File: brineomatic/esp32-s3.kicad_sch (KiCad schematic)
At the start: 37 parts, among them J19 USB_TYPE_C_16PIN, J20 Conn_01x04, U5 ESP32-S3-WROOM-1-N16R8, U6 USBLC6-2SC6, U7 LDL1117S33R, U8 SN74LV1T34DBV

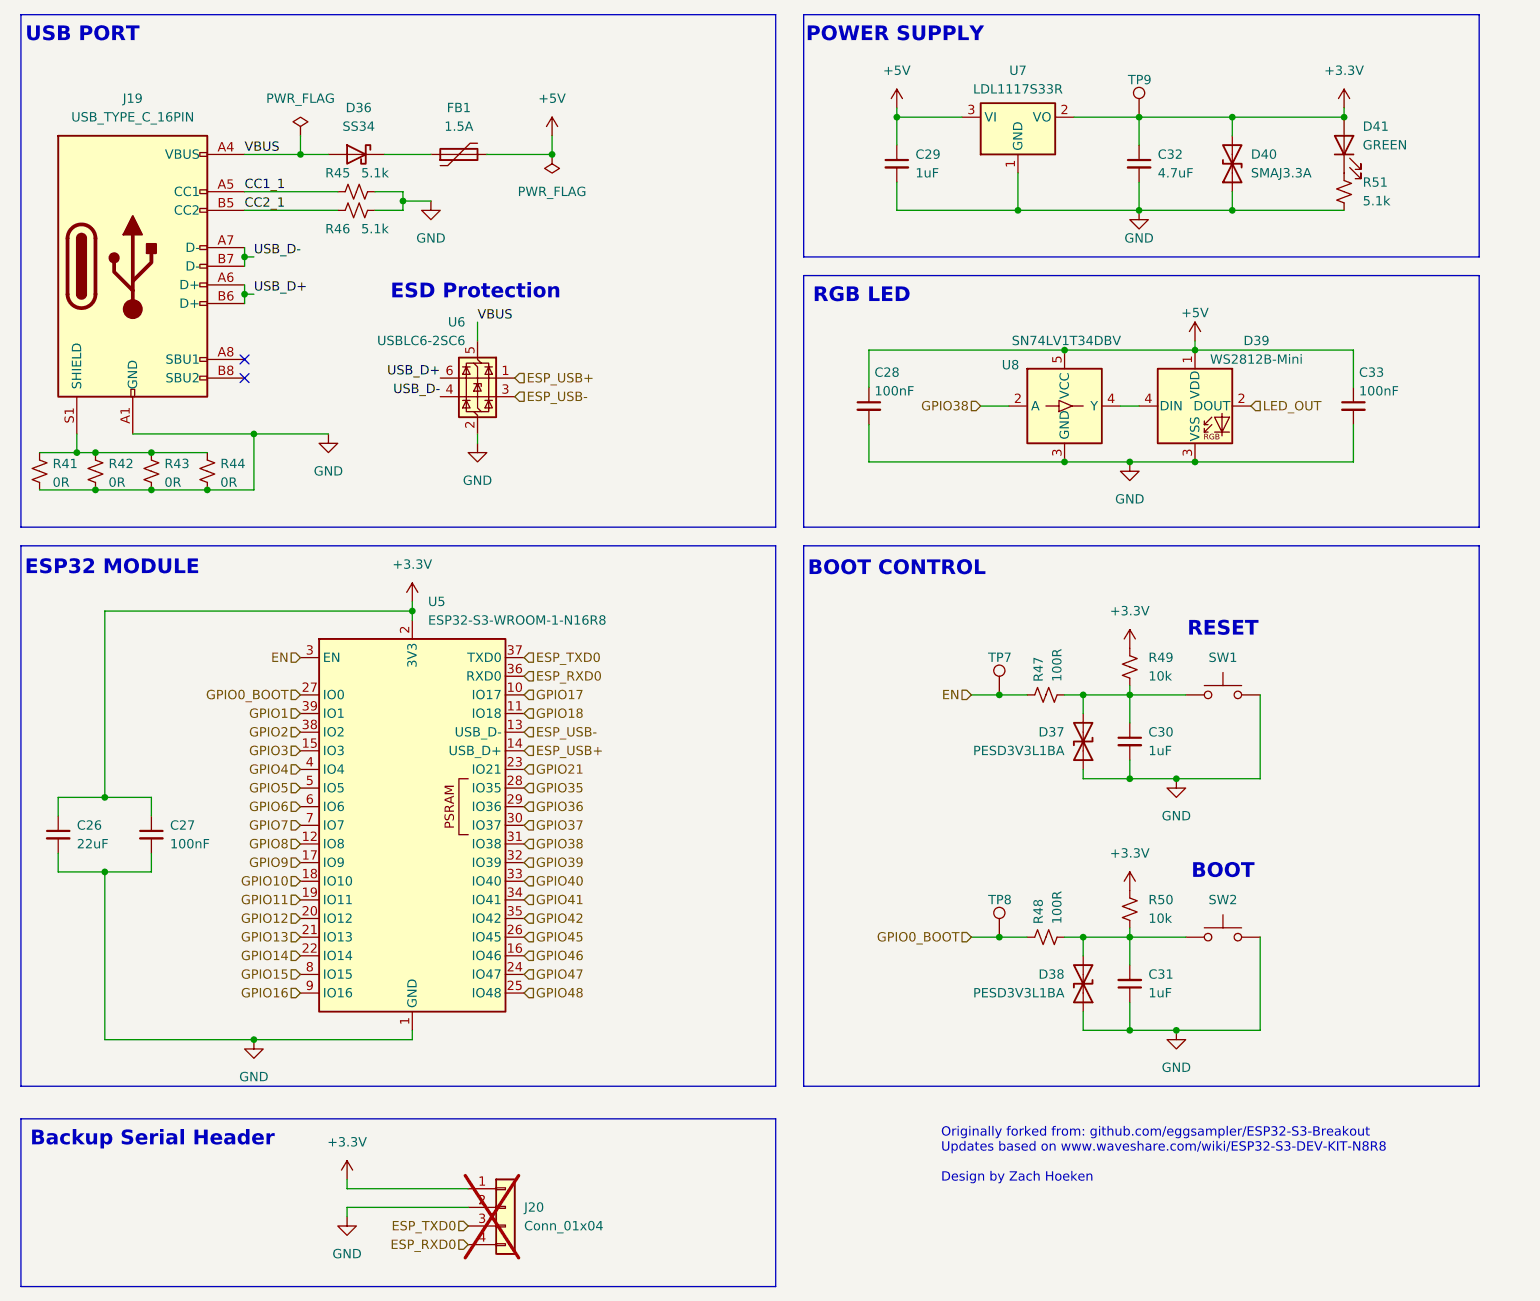
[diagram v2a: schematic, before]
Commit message: updated analog sensor esd schematic
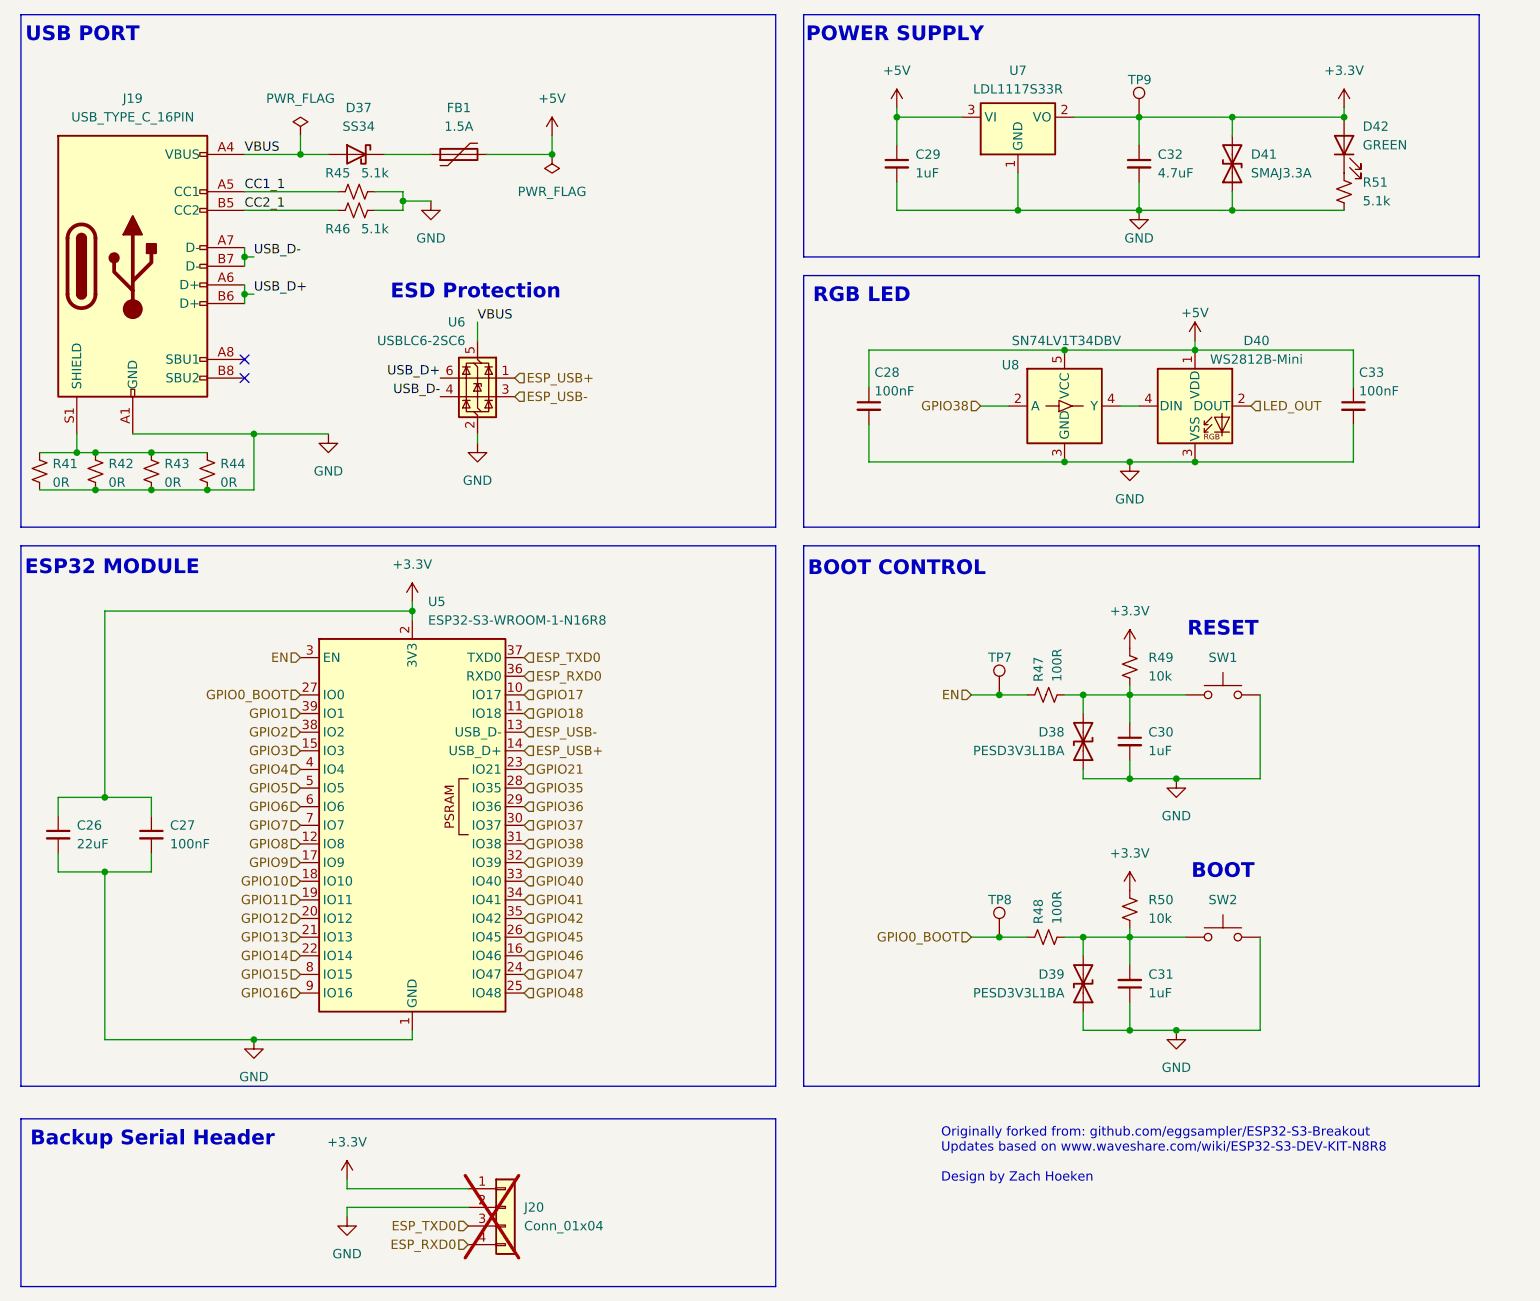
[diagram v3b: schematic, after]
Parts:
- renumbered D36 to D37, D37 to D38, D38 to D39, D39 to D40, D40 to D41, D41 to D42
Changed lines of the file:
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@@
 		(on_board yes)
 		(dnp no)
-		(property "Reference" "#PWR046"
+		(property "Reference" "#PWR047"
 			(at 97.79 179.07 0)
 			(effects
@@
 			(project "brineomatic"
 				(path "/96477ae2-ef08-48f3-8dd4-fe4478541f68/602af921-0504-453c-a784-e82800e98f4c"
-					(reference "#PWR046")
+					(reference "#PWR047")
 					(unit 1)
 				)
@@
 		(on_board yes)
 		(dnp no)
-		(property "Reference" "#PWR054"
+		(property "Reference" "#PWR055"
 			(at 204.47 106.68 0)
 			(effects
@@
 			(project "brineomatic"
 				(path "/96477ae2-ef08-48f3-8dd4-fe4478541f68/602af921-0504-453c-a784-e82800e98f4c"
-					(reference "#PWR054")
+					(reference "#PWR055")
 					(unit 1)
 				)
@@
 		(on_board yes)
 		(dnp no)
-		(property "Reference" "D40"
+		(property "Reference" "D41"
 			(at 220.98 35.56 90)
 			(effects
@@
 			(project "brineomatic"
 				(path "/96477ae2-ef08-48f3-8dd4-fe4478541f68/602af921-0504-453c-a784-e82800e98f4c"
-					(reference "D40")
+					(reference "D41")
 					(unit 1)
 				)
@@
 		(dnp no)
 		(fields_autoplaced yes)
-		(property "Reference" "#PWR050"
+		(property "Reference" "#PWR051"
 			(at 115.57 81.28 0)
 			(effects
@@
 			(project "brineomatic"
 				(path "/96477ae2-ef08-48f3-8dd4-fe4478541f68/602af921-0504-453c-a784-e82800e98f4c"
-					(reference "#PWR050")
+					(reference "#PWR051")
 					(unit 1)
 				)
@@
 		(on_board yes)
 		(dnp no)
-		(property "Reference" "#PWR052"
+		(property "Reference" "#PWR053"
 			(at 172.72 33.02 0)
 			(effects
@@
 			(project "brineomatic"
 				(path "/96477ae2-ef08-48f3-8dd4-fe4478541f68/602af921-0504-453c-a784-e82800e98f4c"
-					(reference "#PWR052")
+					(reference "#PWR053")
 					(unit 1)
 				)
@@
 		(on_board yes)
 		(dnp no)
-		(property "Reference" "#PWR059"
+		(property "Reference" "#PWR060"
 			(at 213.36 64.77 0)
 			(effects
@@
 			(project "brineomatic"
 				(path "/96477ae2-ef08-48f3-8dd4-fe4478541f68/602af921-0504-453c-a784-e82800e98f4c"
-					(reference "#PWR059")
+					(reference "#PWR060")
 					(unit 1)
 				)
@@
 		(on_board yes)
 		(dnp no)
-		(property "Reference" "D38"
+		(property "Reference" "D39"
 			(at 195.58 147.3199 90)
 			(effects
@@
 			(project "brineomatic"
 				(path "/96477ae2-ef08-48f3-8dd4-fe4478541f68/602af921-0504-453c-a784-e82800e98f4c"
-					(reference "D38")
+					(reference "D39")
 					(unit 1)
 				)
@@
 		(on_board yes)
 		(dnp no)
-		(property "Reference" "#PWR055"
+		(property "Reference" "#PWR056"
 			(at 204.47 139.7 0)
 			(effects
@@
 			(project "brineomatic"
 				(path "/96477ae2-ef08-48f3-8dd4-fe4478541f68/602af921-0504-453c-a784-e82800e98f4c"
-					(reference "#PWR055")
+					(reference "#PWR056")
 					(unit 1)
 				)
@@
 		(dnp no)
 		(fields_autoplaced yes)
-		(property "Reference" "#PWR047"
+		(property "Reference" "#PWR048"
 			(at 97.79 186.69 0)
 			(effects
@@
 			(project "brineomatic"
 				(path "/96477ae2-ef08-48f3-8dd4-fe4478541f68/602af921-0504-453c-a784-e82800e98f4c"
-					(reference "#PWR047")
+					(reference "#PWR048")
 					(unit 1)
 				)
@@
 		(dnp no)
 		(fields_autoplaced yes)
-		(property "Reference" "#PWR044"
+		(property "Reference" "#PWR045"
 			(at 85.09 162.56 0)
 			(effects
@@
 			(project "brineomatic"
 				(path "/96477ae2-ef08-48f3-8dd4-fe4478541f68/602af921-0504-453c-a784-e82800e98f4c"
-					(reference "#PWR044")
+					(reference "#PWR045")
 					(unit 1)
 				)
@@
 		(dnp no)
 		(fields_autoplaced yes)
-		(property "Reference" "#PWR053"
+		(property "Reference" "#PWR054"
 			(at 204.47 83.82 0)
 			(effects
@@
 			(project "brineomatic"
 				(path "/96477ae2-ef08-48f3-8dd4-fe4478541f68/602af921-0504-453c-a784-e82800e98f4c"
-					(reference "#PWR053")
+					(reference "#PWR054")
 					(unit 1)
 				)
@@
 		(on_board yes)
 		(dnp no)
-		(property "Reference" "D36"
+		(property "Reference" "D37"
 			(at 99.3775 29.21 0)
 			(effects
@@
 			(project "brineomatic"
 				(path "/96477ae2-ef08-48f3-8dd4-fe4478541f68/602af921-0504-453c-a784-e82800e98f4c"
-					(reference "D36")
+					(reference "D37")
 					(unit 1)
 				)
@@
 		(dnp no)
 		(fields_autoplaced yes)
-		(property "Reference" "#PWR057"
+		(property "Reference" "#PWR058"
 			(at 210.82 127 0)
 			(effects
@@
 			(project "brineomatic"
 				(path "/96477ae2-ef08-48f3-8dd4-fe4478541f68/602af921-0504-453c-a784-e82800e98f4c"
-					(reference "#PWR057")
+					(reference "#PWR058")
 					(unit 1)
 				)
@@
 		(dnp no)
 		(fields_autoplaced yes)
-		(property "Reference" "#PWR058"
+		(property "Reference" "#PWR059"
 			(at 210.82 161.29 0)
 			(effects
@@
 			(project "brineomatic"
 				(path "/96477ae2-ef08-48f3-8dd4-fe4478541f68/602af921-0504-453c-a784-e82800e98f4c"
-					(reference "#PWR058")
+					(reference "#PWR059")
 					(unit 1)
 				)
@@
 		(on_board yes)
 		(dnp no)
-		(property "Reference" "D39"
+		(property "Reference" "D40"
 			(at 221.742 60.96 0)
 			(effects
@@
 			(project "brineomatic"
 				(path "/96477ae2-ef08-48f3-8dd4-fe4478541f68/602af921-0504-453c-a784-e82800e98f4c"
-					(reference "D39")
+					(reference "D40")
 					(unit 1)
 				)
@@
 		(dnp no)
 		(fields_autoplaced yes)
-		(property "Reference" "#PWR049"
+		(property "Reference" "#PWR050"
 			(at 109.22 48.26 0)
 			(effects
@@
 			(project "brineomatic"
 				(path "/96477ae2-ef08-48f3-8dd4-fe4478541f68/602af921-0504-453c-a784-e82800e98f4c"
-					(reference "#PWR049")
+					(reference "#PWR050")
 					(unit 1)
 				)
@@
 		(on_board yes)
 		(dnp no)
-		(property "Reference" "#PWR048"
+		(property "Reference" "#PWR049"
 			(at 106.68 100.33 0)
 			(effects
@@
 			(project "brineomatic"
 				(path "/96477ae2-ef08-48f3-8dd4-fe4478541f68/602af921-0504-453c-a784-e82800e98f4c"
-					(reference "#PWR048")
+					(reference "#PWR049")
 					(unit 1)
 				)
@@
 		(on_board yes)
 		(dnp no)
-		(property "Reference" "#PWR060"
+		(property "Reference" "#PWR061"
 			(at 233.68 33.02 0)
 			(effects
@@
 			(project "brineomatic"
 				(path "/96477ae2-ef08-48f3-8dd4-fe4478541f68/602af921-0504-453c-a784-e82800e98f4c"
-					(reference "#PWR060")
+					(reference "#PWR061")
 					(unit 1)
 				)
@@
 		(on_board yes)
 		(dnp no)
-		(property "Reference" "D41"
+		(property "Reference" "D42"
 			(at 236.22 31.75 90)
 			(effects
@@
 			(project "brineomatic"
 				(path "/96477ae2-ef08-48f3-8dd4-fe4478541f68/602af921-0504-453c-a784-e82800e98f4c"
-					(reference "D41")
+					(reference "D42")
 					(unit 1)
 				)
@@
 		(dnp no)
 		(fields_autoplaced yes)
-		(property "Reference" "#PWR045"
+		(property "Reference" "#PWR046"
 			(at 95.25 80.01 0)
 			(effects
@@
 			(project "brineomatic"
 				(path "/96477ae2-ef08-48f3-8dd4-fe4478541f68/602af921-0504-453c-a784-e82800e98f4c"
-					(reference "#PWR045")
+					(reference "#PWR046")
 					(unit 1)
 				)
@@
 		(on_board yes)
 		(dnp no)
-		(property "Reference" "#PWR051"
+		(property "Reference" "#PWR052"
 			(at 125.73 36.83 0)
 			(effects
@@
 			(project "brineomatic"
 				(path "/96477ae2-ef08-48f3-8dd4-fe4478541f68/602af921-0504-453c-a784-e82800e98f4c"
-					(reference "#PWR051")
+					(reference "#PWR052")
 					(unit 1)
 				)
@@
 		(on_board yes)
 		(dnp no)
-		(property "Reference" "#PWR056"
+		(property "Reference" "#PWR057"
 			(at 205.74 49.53 0)
 			(effects
@@
 			(project "brineomatic"
 				(path "/96477ae2-ef08-48f3-8dd4-fe4478541f68/602af921-0504-453c-a784-e82800e98f4c"
-					(reference "#PWR056")
+					(reference "#PWR057")
 					(unit 1)
 				)
@@
 		(on_board yes)
 		(dnp no)
-		(property "Reference" "D37"
+		(property "Reference" "D38"
 			(at 195.58 114.2999 90)
 			(effects
@@
 			(project "brineomatic"
 				(path "/96477ae2-ef08-48f3-8dd4-fe4478541f68/602af921-0504-453c-a784-e82800e98f4c"
-					(reference "D37")
+					(reference "D38")
 					(unit 1)
 				)

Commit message: added bulk cap after ideal diode
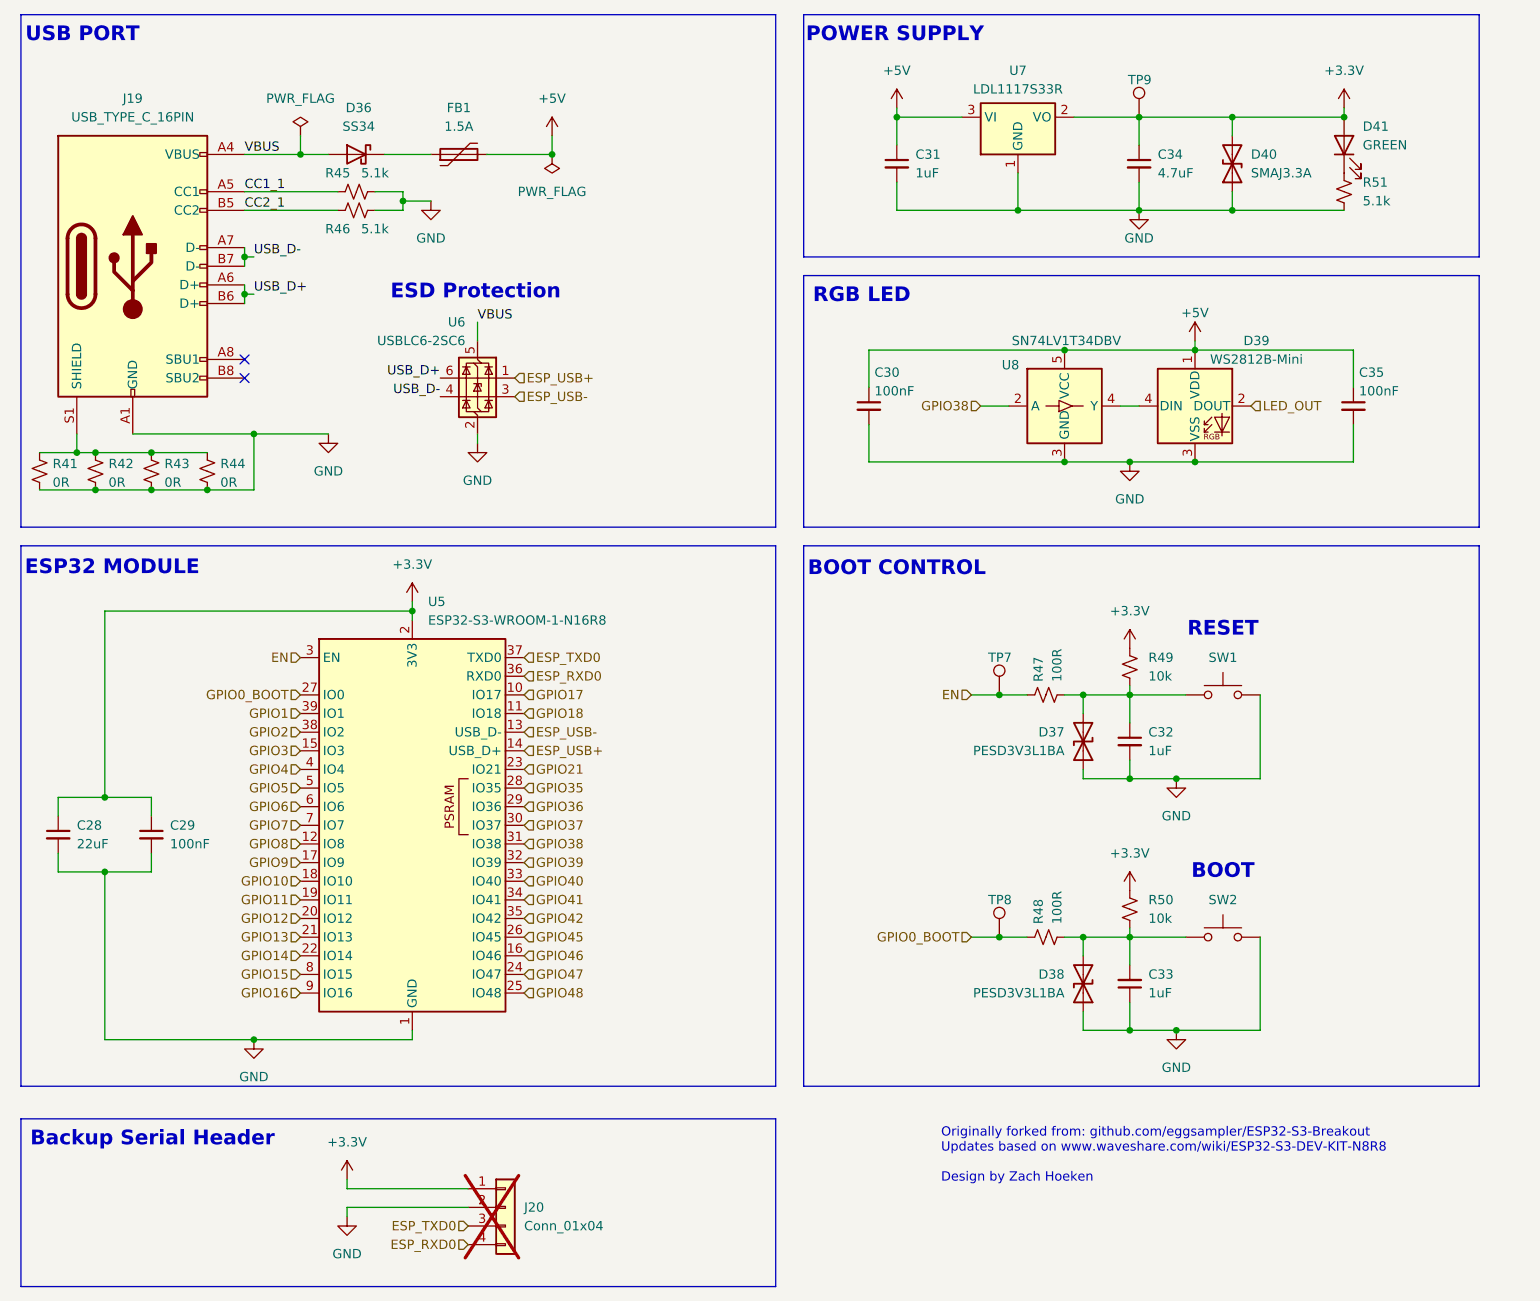
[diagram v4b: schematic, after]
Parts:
- renumbered C26 to C28, C27 to C29, C28 to C30, C29 to C31, C30 to C32, C31 to C33, C32 to C34, C33 to C35, D37 to D36, D38 to D37, D39 to D38, D40 to D39, D41 to D40, D42 to D41
